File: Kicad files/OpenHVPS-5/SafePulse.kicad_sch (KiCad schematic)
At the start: 86 parts, among them J1 Conn_01x03_Male, Q1 FQT7N10L, Q2 BC846A, Q3 MMBT3906, Q4 MMBT3906, U1 TS4061AILT-1.25, U2 74HC14, U3 MAX9910EXK+T, U4 CD14538BM

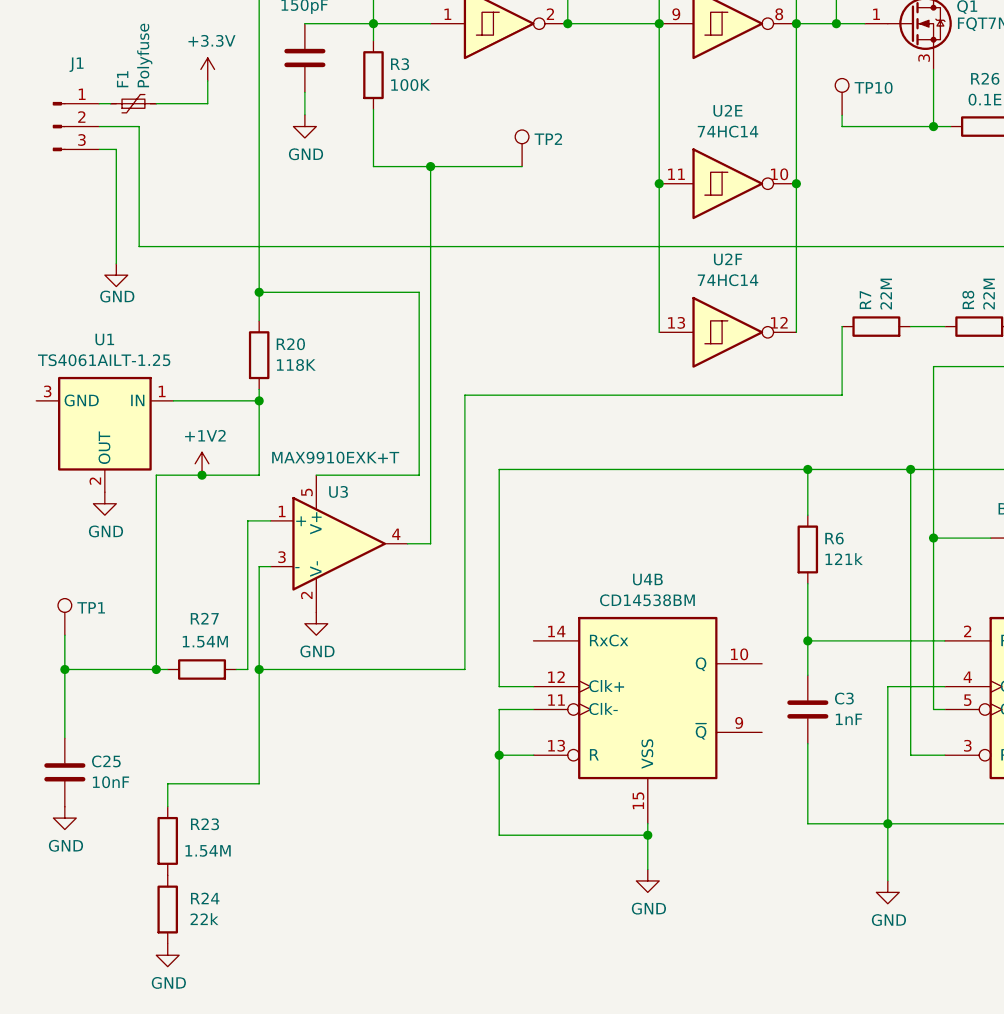
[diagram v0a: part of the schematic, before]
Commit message: Added parts list for JLPCB
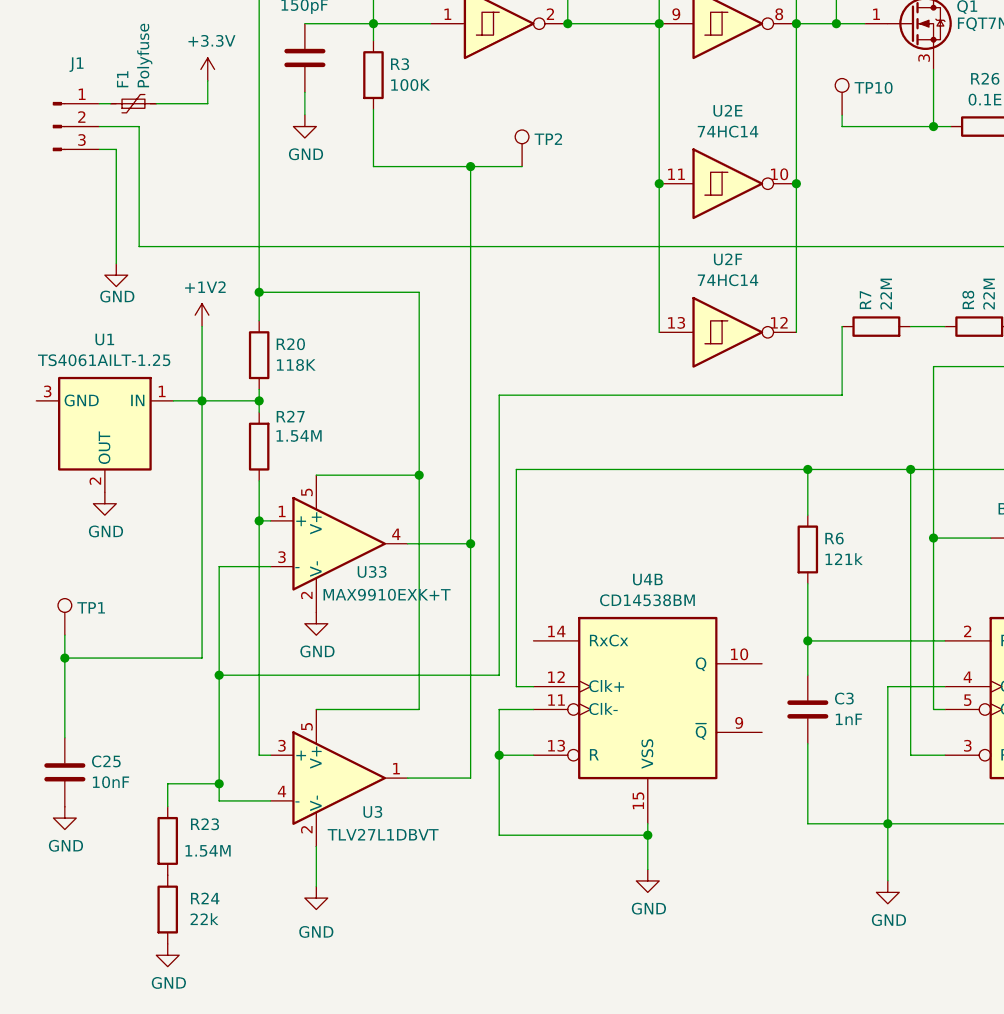
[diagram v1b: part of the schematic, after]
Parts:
- added U3: TLV27L1DBVT, Package_TO_SOT_SMD:SOT-23-5, symbol Amplifier_Operational:TLV2371DBV
- C1: LCSC Part # (none) -> C520084
- C10, C11, C12, C13, C14, C15, C16, C17, C18, C6, C7, C8, C9: LCSC Part # (none) -> C710458
- C19, C2, C23, C27, C5: LCSC Part # (none) -> C1713
- C22: LCSC Part # (none) -> C1818
- C24, C25: LCSC Part # (none) -> C97905
- C3: LCSC Part # (none) -> C277515
- C4: LCSC Part # (none) -> C525654
- D1, D2: LCSC Part # (none) -> C282360
- D3, D4, D5, D6, D7, D8, D9: LCSC Part # (none) -> C151049
- F1: LCSC Part # (none) -> C20978
- FB1, FB2: LCSC Part # (none) -> C515370
- L1: LCSC Part # (none) -> C2043159
- Q1: LCSC Part # (none) -> C154506
- Q2: LCSC Part # (none) -> C507907
- Q3, Q4: LCSC Part # (none) -> C53444
- R1: LCSC Part # (none) -> C488845
- R10, R7, R8, R9: LCSC Part # (none) -> C34719
- R11: LCSC Part # (none) -> C242487
- R12, R25, R5: LCSC Part # (none) -> C328380
- R13, R19, R3: LCSC Part # (none) -> C96346
- R14: LCSC Part # (none) -> C325883
- R15: LCSC Part # (none) -> C104108
- R16: LCSC Part # (none) -> C107700
- R17: LCSC Part # (none) -> C317482
- R18: LCSC Part # (none) -> C95781
- R20: LCSC Part # (none) -> C228266
- R21: LCSC Part # (none) -> C328397
- R22: LCSC Part # (none) -> C163977
- R23, R27: LCSC Part # (none) -> C332788
- R24: LCSC Part # (none) -> C352242
- R26: LCSC Part # (none) -> C346794
- R4: LCSC Part # (none) -> C161788
- R6: LCSC Part # (none) -> C844393
- U1: LCSC Part # (none) -> C2157484
- U2: LCSC Part # (none) -> C232776
- U33: renamed from U3; LCSC Part # (none) -> C2057992
- U4: LCSC Part # (none) -> C2652506
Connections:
- net +1V2: now also R27.2; no longer R27.1
- net GND: now also U3.2 (V-)
- net at R23.1, R7.1, U33.3 (-): now also U3.4 (-)
- net at C27.1, R20.1, R25.2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: now also U3.5 (V+)
- net at R3.2, TP2.1, U33.4: now also U3.1
- net at U33.1 (+): now also R27.1, U3.3 (+); no longer R27.2
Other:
- moved on the sheet: R27
